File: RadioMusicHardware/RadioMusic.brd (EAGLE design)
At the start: 106 x 49 mm, 63 parts, among them IC2 7805L, IC3 TL072P, IC4 TL072P

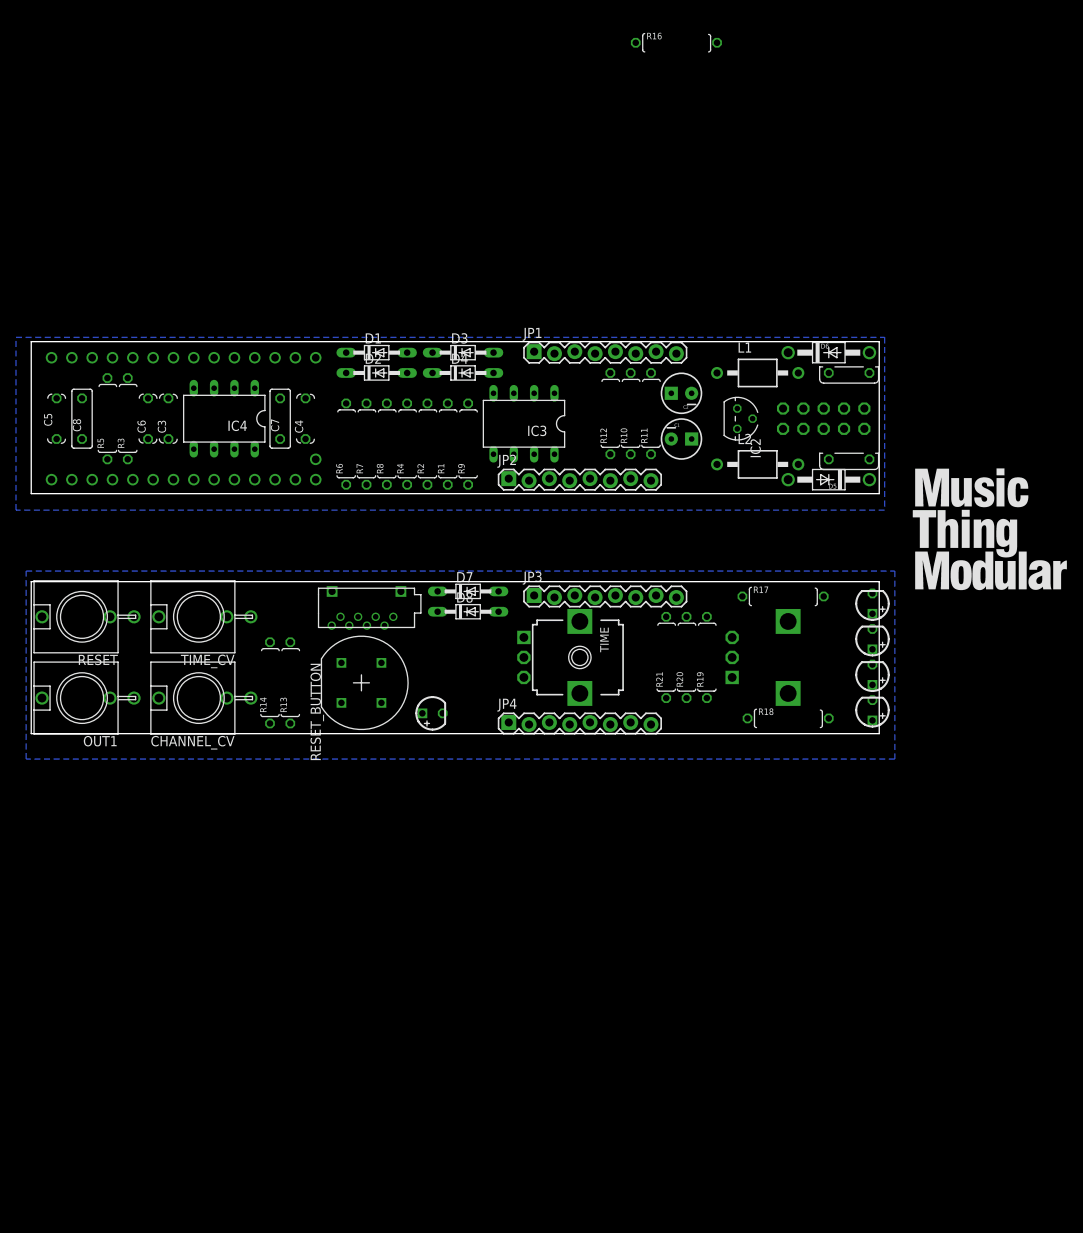
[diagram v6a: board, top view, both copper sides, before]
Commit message: split signals across back and front
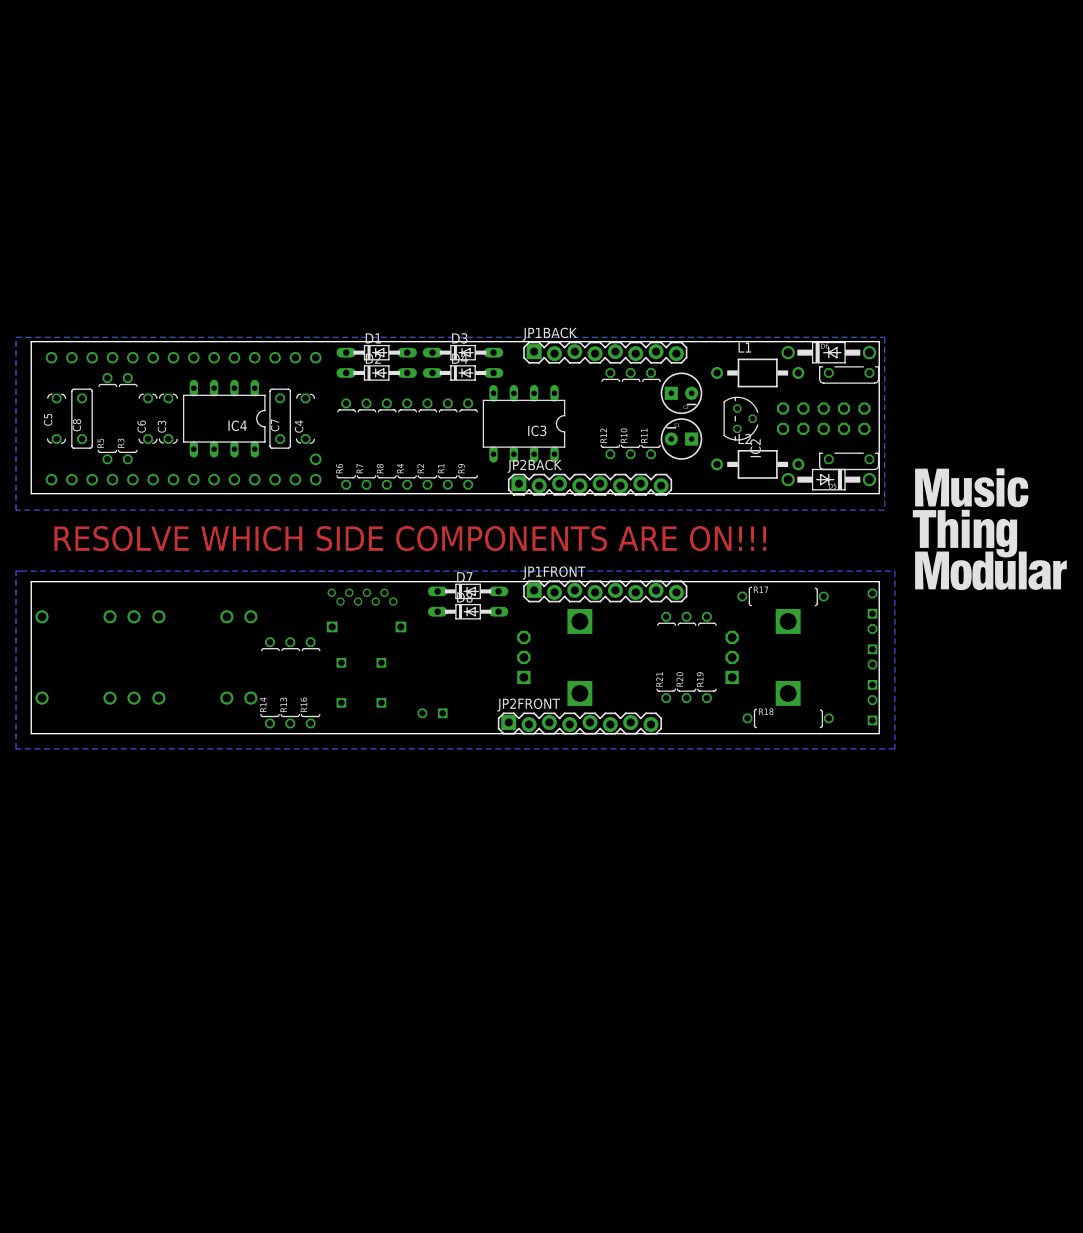
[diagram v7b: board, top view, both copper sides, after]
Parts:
- removed JP2, JP3: (no value), SparkFun-Connectors:1X08_LOCK
- added JP1FRONT, JP2BACK: (no value), SparkFun-Connectors:1X08_LOCK
- moved R16 92.2 mm to (34.9, 6.35), turned to 90 degrees
- moved U$3 1.91 mm to (41.9, 16.5), flipped to the bottom, turned to 0 degrees
- flipped CHANNEL_CV to the bottom, turned to 270 degrees
- flipped LED1 to the bottom
- flipped LED2 to the bottom
- flipped LED3 to the bottom
- flipped LED4 to the bottom
- flipped OUT1 to the bottom, turned to 270 degrees
- flipped RESET to the bottom, turned to 270 degrees
- flipped RESET_BUTTON to the bottom
- flipped RESET_LED to the bottom
- flipped TIME to the bottom, turned to 90 degrees
- flipped TIME_CV to the bottom, turned to 270 degrees
- renumbered JP1 to JP1BACK, JP4 to JP2FRONT
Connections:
- removed net N$1: CHANNEL_CV.P$1, R1.1, R2.2
- removed net N$11: R10.1, R11.2, TIME_CV.P$1
- removed net N$13: LED1.A, U$1.3
- removed net N$15: LED2.A, U$1.4
- removed net N$16: LED3.A, U$1.5
- removed net N$17: LED4.A, U$1.6
- removed net N$24: RESET_LED.A, U$1.11
- removed net N$9: OUT1.P$1, R4.2
- removed net PIN2: U$1.2
- removed net PIN21/A7: TIME.2, U$1.21/A7
- removed net PIN23/A9: CHANNEL.2, U$1.23/A9
- removed net PIN8: R16.2, RESET_BUTTON.P$1, RESET_BUTTON.P$2, U$1.8
- removed net PIN9: D7.A, D8.C, R13.2, R14.2, U$1.9
- new net +3.3V_F: CHANNEL.3, D7.C, JP1FRONT.7, RESET_BUTTON.P$3, RESET_BUTTON.P$4, TIME.3, U$3.P$4
- new net AUDIO_OUT: JP2BACK.3, R4.2
- new net AUDIO_OUT_F: JP2FRONT.3, OUT1.P$1
- new net CHANNEL_CV: JP2BACK.6, R1.1, R2.2
- new net CHANNEL_CV_F: CHANNEL_CV.P$1, JP2FRONT.6
- new net CHANNEL_POT: JP2BACK.5, U$1.23/A9
- new net CHANNEL_POT_F: CHANNEL.2, JP2FRONT.5
- new net GND_F: CHANNEL.1, CHANNEL_CV.P$3, D8.A, JP1FRONT.8, OUT1.P$3, R13.1, R16.1, R17.1, R18.1, R19.1, R20.1, R21.1, RESET.P$3, TIME.1, TIME_CV.P$3, U$3.GND1, U$3.GND2, U$3.P$6
- new net LED1: JP1BACK.6, U$1.3
- new net LED1_F: JP1FRONT.6, LED1.A
- new net LED2: JP1BACK.5, U$1.4
- new net LED2_F: JP1FRONT.5, LED2.A
- new net LED3: JP1BACK.4, U$1.5
- new net LED3_F: JP1FRONT.4, LED3.A
- new net LED4: JP1BACK.3, U$1.6
- new net LED4_F: JP1FRONT.3, LED4.A
- new net LED_RESET: JP1BACK.2, U$1.11
- new net LED_RESET_F: JP1FRONT.2, RESET_LED.A
- new net MISO_F: U$3.P$7
- new net MOSI_F: U$3.P$3
- new net N$40: JP2BACK.2
- new net N$41: JP2BACK.1
- new net N$42: JP2FRONT.1
- new net N$43: JP2FRONT.2
- new net RESET_CV: JP2BACK.8, U$1.9
- new net RESET_CV_F: D7.A, D8.C, JP2FRONT.8, R13.2, R14.2
- new net RESET_SW: JP1BACK.1, U$1.8
- new net RESET_SW_F: JP1FRONT.1, R16.2, RESET_BUTTON.P$1, RESET_BUTTON.P$2
- new net SCLK_F: U$3.P$5
- new net SS_F: U$3.P$2
- new net TIME_CV: JP2BACK.7, R10.1, R11.2
- new net TIME_CV_F: JP2FRONT.7, TIME_CV.P$1
- new net TIME_POT: JP2BACK.4, U$1.21/A7
- new net TIME_POT_F: JP2FRONT.4, TIME.2
- net +3.3V: now also JP1BACK.7; no longer CHANNEL.3, D7.C, RESET_BUTTON.P$3, RESET_BUTTON.P$4, TIME.3, U$3.P$4
- net GND: now also JP1BACK.8; no longer CHANNEL.1, CHANNEL_CV.P$3, D8.A, OUT1.P$3, R13.1, R16.1, R17.1, R18.1, R19.1, R20.1, R21.1, RESET.P$3, TIME.1, TIME_CV.P$3, U$3.GND1, U$3.GND2, U$3.P$6
- net MISO: no longer U$3.P$7
- net MOSI: no longer U$3.P$3
- net SCLK: no longer U$3.P$5
- net SS: no longer U$3.P$2
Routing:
- added copper zone on layer 16, net GND_F
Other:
- board text added: "RESOLVE WHICH SIDE COMPONENTS ARE ON!!!"

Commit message: Simple Crossfading
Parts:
- JP2BACK, JP2FRONT: value (none) -> M10LOCK; device SparkFun-Connectors:1X08_LOCK -> SparkFun-Connectors:1X10_LOCK
- moved IC2 81.9 mm to (6.35, 40.0), turned to 90 degrees
- moved R12 45.1 mm to (27.3, 38.7)
- moved R9 40.8 mm to (14.0, 39.4)
- moved IC3 40.6 mm to (21.0, 39.4)
- moved D1 35.1 mm to (8.89, 40.0), turned to 90 degrees
- moved IC4 33.7 mm to (57.8, 39.4)
- moved C8 32.8 mm to (38.7, 34.3)
- moved D2 32.2 mm to (11.4, 40.0), turned to 90 degrees
- moved C4 31.9 mm to (2.54, 36.1), turned to 270 degrees
- moved R3 31.8 mm to (43.8, 39.4)
- moved R5 31.8 mm to (41.3, 39.4)
- moved C6 31.4 mm to (45.1, 31.8), turned to 180 degrees
- moved C3 29.2 mm to (46.4, 39.4), turned to 270 degrees
- moved D4 24.8 mm to (29.8, 39.4), turned to 90 degrees
- moved D3 23.1 mm to (32.4, 39.4), turned to 90 degrees
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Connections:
- removed net AGND: U$1.AGND
- removed net N$40: JP2BACK.2
- removed net N$41: JP2BACK.1
- removed net N$42: JP2FRONT.1
- removed net N$43: JP2FRONT.2
- new net DGND: C4.2, C5.2, D2.A, D4.A, IC2.2, U$1.GND
- new net N$1: IC3.6, IC3.7, R12.1
- net +12V: now also L1.1; no longer L1.2
- net +3.3V: now also JP2BACK.1; no longer JP1BACK.7
- net +3.3V_F: now also JP2FRONT.1; no longer JP1FRONT.7
- net -12V: now also C5.1, L2.1; no longer C5.2, L2.2
- net AUDIO_OUT: now also JP2BACK.5, R4.1; no longer JP2BACK.3, R4.2
- net AUDIO_OUT_F: now also JP2FRONT.5; no longer JP2FRONT.3
- net CHANNEL_CV: now also JP2BACK.8, R2.1; no longer JP2BACK.6, R2.2
- net CHANNEL_CV_F: now also JP2FRONT.8; no longer JP2FRONT.6
- net CHANNEL_POT: now also JP2BACK.7; no longer JP2BACK.5
- net CHANNEL_POT_F: now also JP2FRONT.7; no longer JP2FRONT.5
- net DAC: now also C8.1; no longer C8.2
- net GND: now also R11.2, R2.2, U$1.AGND; no longer C4.2, C5.1, D2.A, D4.A, IC2.2, R11.1, R2.1, U$1.GND
- net MISO: now also JP2BACK.4
- net MISO_F: now also JP2FRONT.4
- net MOSI: now also JP2BACK.3
- net MOSI_F: now also JP2FRONT.3
- net N$10: now also C8.2; no longer C8.1
- net N$2: now also IC4.5, R3.1; no longer IC4.3, R3.2
- net N$22: now also L1.2; no longer L1.1
- net N$23: now also L2.2; no longer L2.1
- net N$4: now also C3.1, R3.2; no longer C3.2, R3.1
- net N$5: now also C3.2, IC4.6, IC4.7; no longer C3.1, IC4.1, IC4.2
- net N$6: now also IC4.3; no longer IC4.5
- net N$7: now also IC4.2, R8.2; no longer IC4.6, R8.1
- net N$8: now also IC4.1, R4.2, R8.1; no longer IC4.7, R4.1, R8.2
- net PIN22/A8: no longer IC3.6, IC3.7, R12.1
- net RESET_CV: now also JP2BACK.10; no longer JP2BACK.8
- net RESET_CV_F: now also JP2FRONT.10; no longer JP2FRONT.8
- net SCLK: now also JP2BACK.2
- net SCLK_F: now also JP2FRONT.2
- net SS: now also JP1BACK.7
- net SS_F: now also JP1FRONT.7
- net TIME_CV: now also JP2BACK.9, R11.1; no longer JP2BACK.7, R11.2
- net TIME_CV_F: now also JP2FRONT.9; no longer JP2FRONT.7
- net TIME_POT: now also JP2BACK.6; no longer JP2BACK.4
- net TIME_POT_F: now also JP2FRONT.6; no longer JP2FRONT.4
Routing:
- added copper zone on layer 16, net DGND
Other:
- board text added: "BACK BOARD: COMPONENTS + JUMPERS ON TOP, POWER AND TEENSY ON BOTTOM FRONT BOARD: POTS, JACKS + COMPONENTS ON TOP, JUMPERS ON BOTTOM"
- board text removed: "RESOLVE WHICH SIDE COMPONENTS ARE ON!!!"
